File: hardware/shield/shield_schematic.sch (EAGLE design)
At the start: 4 parts, among them IC1 7805TV

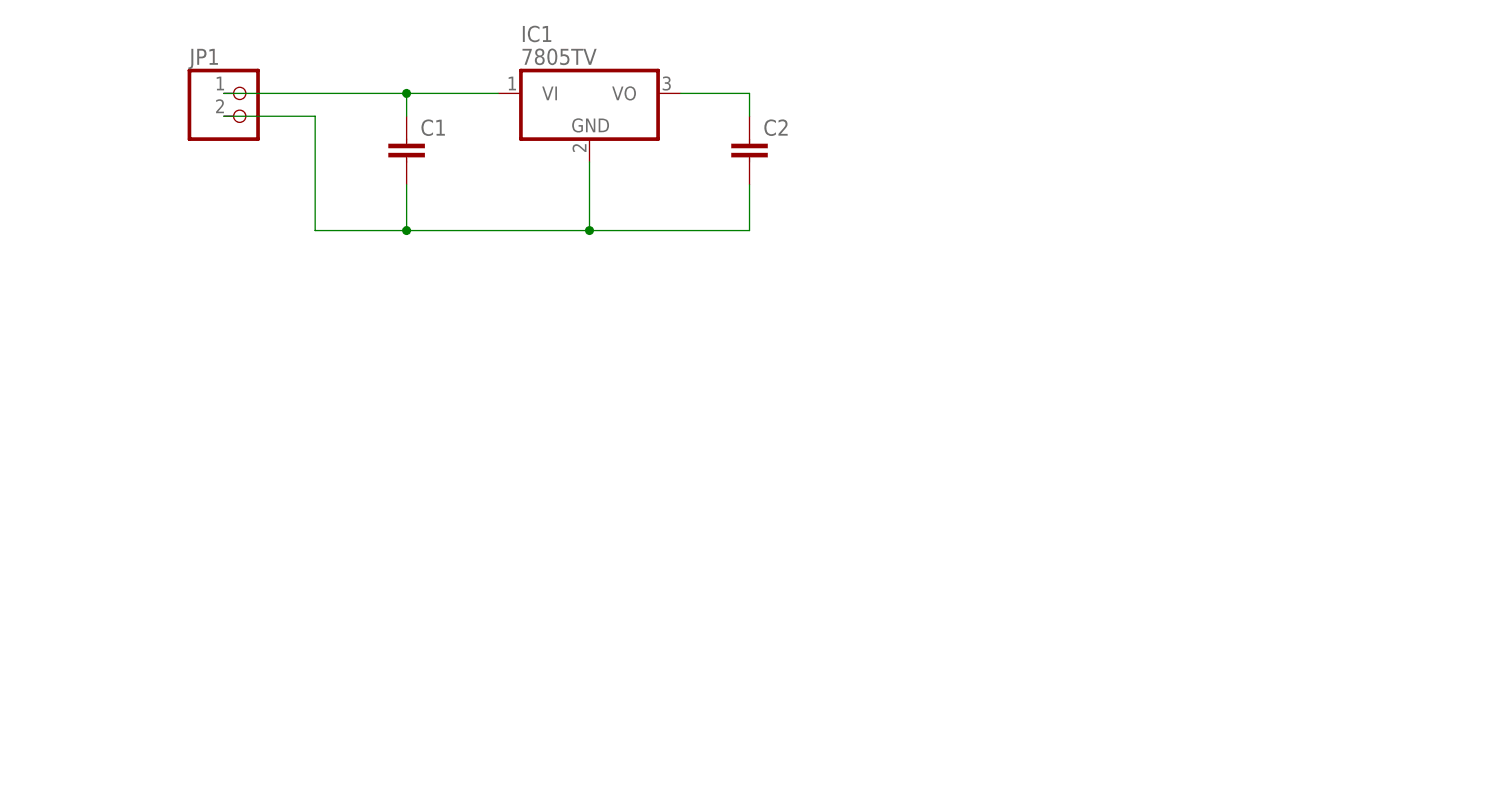
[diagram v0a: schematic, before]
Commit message: Updating the schematics to include A5 frames and complete some component values. Also adding the arduino shield symbol to the shield schematic.
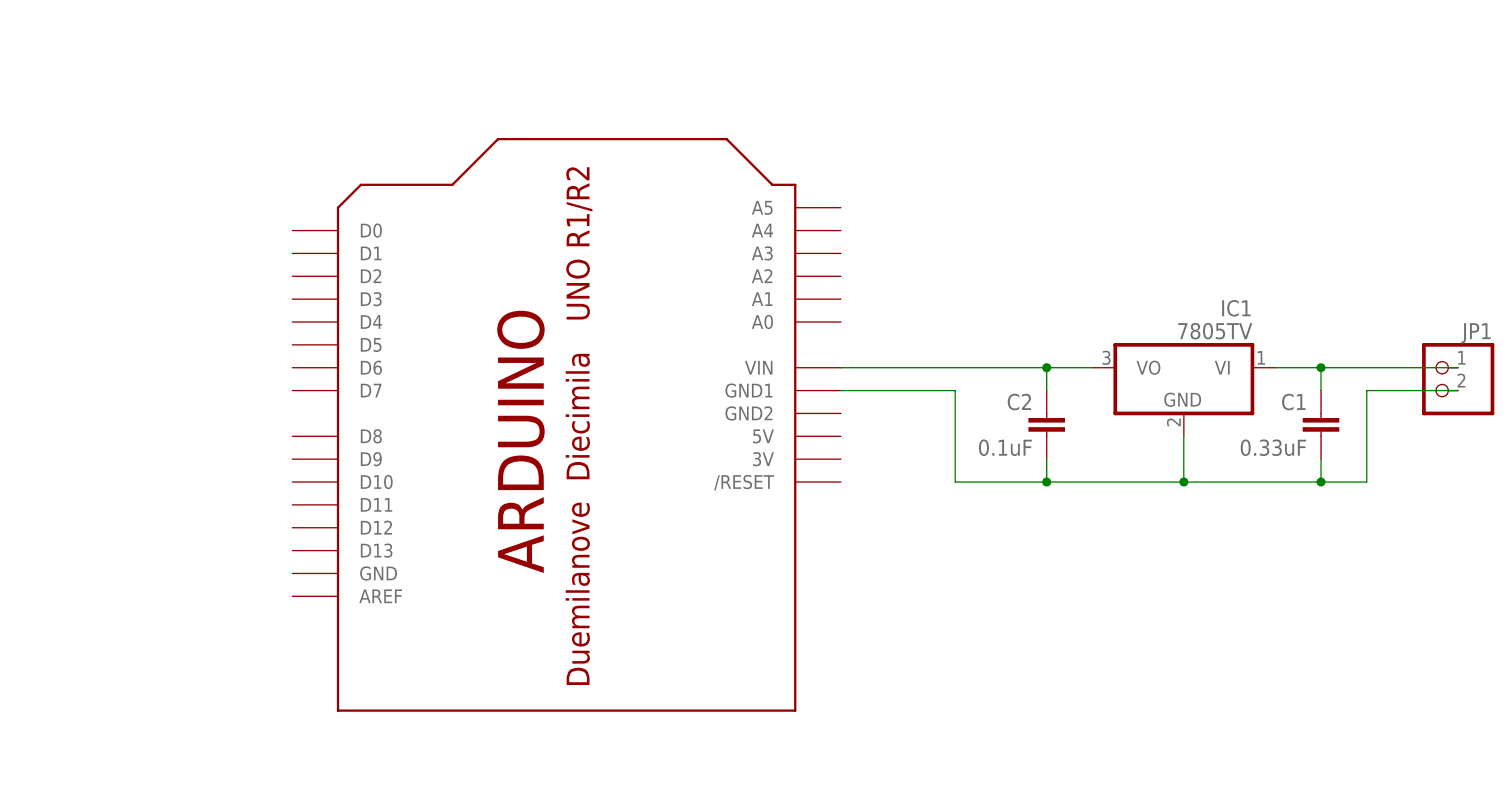
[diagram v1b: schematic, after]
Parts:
- added U$1: ARDUINO-BPLACE, adafruit:ARDUINO-BPLACE
- C1: value (none) -> 0.33uF
- C2: value (none) -> 0.1uF
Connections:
- net N$2: now also U$1.GND1
- net N$3: now also U$1.VIN
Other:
- moved on the sheet: C1, C2, IC1, JP1

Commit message: Update shield schematic: Only uses a single 3.3V regulator. Added the I2C connector and pull ups. Added a note to the SDA UART RX (uC TX) pin used for debugging.
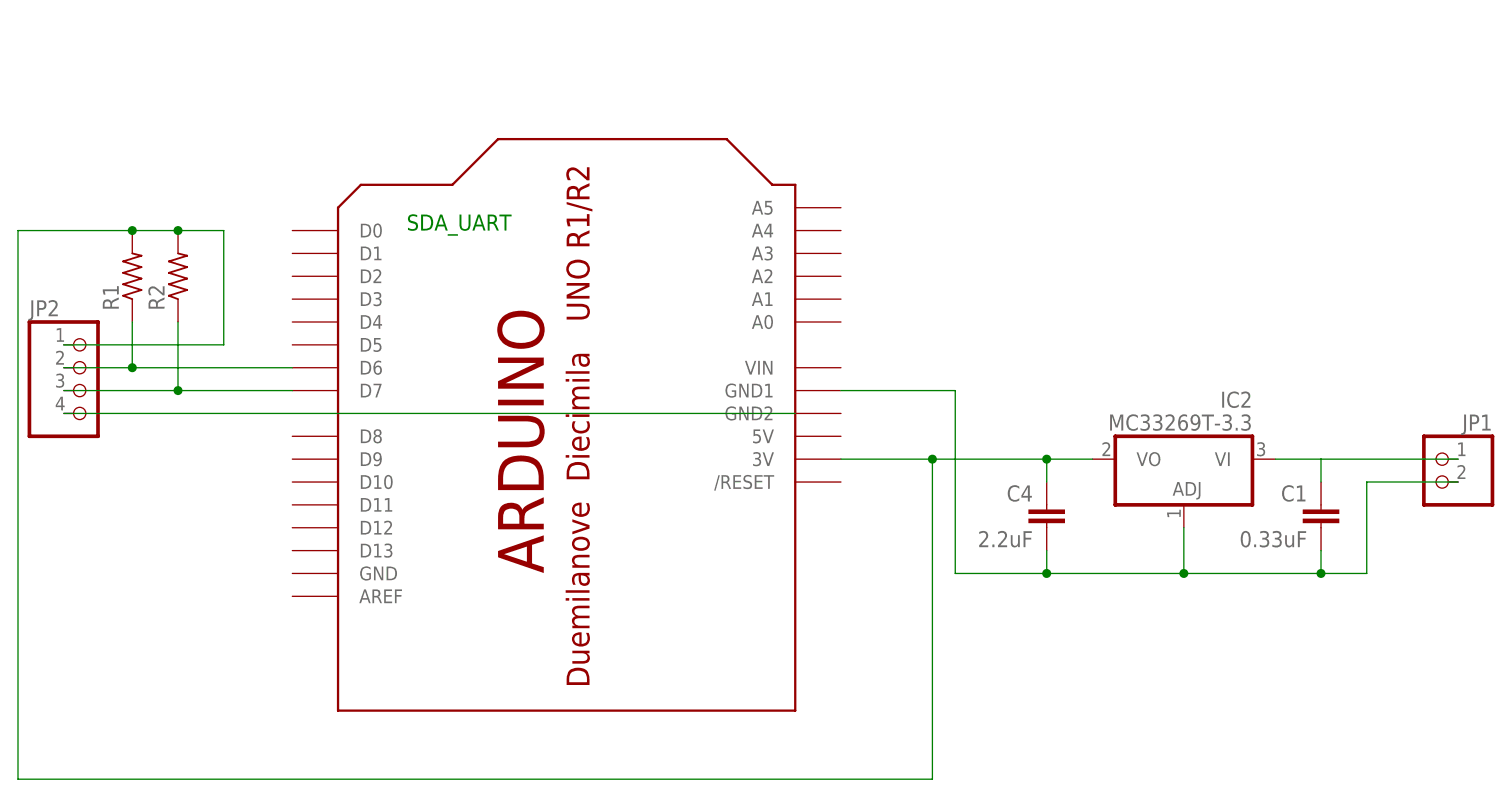
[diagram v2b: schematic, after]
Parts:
- removed C2: 0.1uF, capacitor-wima:C5/2.5
- removed IC1: 7805TV, linear:7805TV
- added C4: 2.2uF, capacitor-wima:C5/2.5
- added IC2: MC33269T-3.3, linear:MC33269T-3.3
- added JP2: (no value), pinhead:PINHD-1X4
- added R1, R2: (no value), resistor:R-US_0204/7
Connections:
- removed net N$3: C2.1, IC1.VO, U$1.VIN
- new net N$4: C4.1, IC2.VO, JP2.1, R1.2, R2.2, U$1.3V
- new net N$5: JP2.2, R1.1, U$1.D6
- new net N$6: JP2.3, R2.1, U$1.D7
- new net N$7: JP2.4
- net N$1: now also IC2.VI; no longer IC1.VI
- net N$2: now also C4.2, IC2.ADJ; no longer C2.2, IC1.GND
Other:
- note added: "SDA_UART"
- moved on the sheet: C1, JP1
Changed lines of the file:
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@@
 </classes>
 <parts>
-<part name="IC1" library="linear" deviceset="78*" device="TV" technology="05"/>
 <part name="C1" library="capacitor-wima" deviceset="C" device="5/2.5" value="0.33uF"/>
-<part name="C2" library="capacitor-wima" deviceset="C" device="5/2.5" value="0.1uF"/>
 <part name="JP1" library="pinhead" deviceset="PINHD-1X2" device=""/>
 <part name="U$1" library="adafruit" deviceset="ARDUINO" device="-BPLACE"/>
 <part name="FRAME2" library="frames" deviceset="DINA5_L" device=""/>
+<part name="IC2" library="linear" deviceset="MC33269?*" device="T" technology="-3.3"/>
+<part name="C4" library="capacitor-wima" deviceset="C" device="5/2.5" value="2.2uF"/>
+<part name="JP2" library="pinhead" deviceset="PINHD-1X4" device=""/>
+<part name="R1" library="resistor" deviceset="R-US_" device="0204/7"/>
+<part name="R2" library="resistor" deviceset="R-US_" device="0204/7"/>
 </parts>
 <sheets>
 <sheet>
 <plain>
+<text x="55.88" y="96.52" size="1.778" layer="91">SDA_UART</text>
 </plain>
 <instances>
-<instance part="IC1" gate="A1" x="142.24" y="81.28" rot="MR0"/>
-<instance part="C1" gate="G$1" x="157.48" y="76.2" rot="MR0"/>
-<instance part="C2" gate="G$1" x="127" y="76.2" rot="MR0"/>
-<instance part="JP1" gate="G$1" x="170.18" y="78.74" rot="MR0"/>
+<instance part="C1" gate="G$1" x="157.48" y="66.04" rot="MR0"/>
+<instance part="JP1" gate="G$1" x="170.18" y="68.58" rot="MR0"/>
 <instance part="U$1" gate="G$1" x="71.12" y="66.04" rot="R90"/>
 <instance part="FRAME2" gate="G$1" x="5.08" y="7.62"/>
+<instance part="IC2" gate="G$1" x="142.24" y="68.58" rot="MR0"/>
+<instance part="C4" gate="G$1" x="127" y="66.04" rot="MR0"/>
+<instance part="JP2" gate="A" x="20.32" y="78.74"/>
+<instance part="R1" gate="G$1" x="25.4" y="91.44" rot="R90"/>
+<instance part="R2" gate="G$1" x="30.48" y="91.44" rot="R90"/>
 </instances>
 <busses>
@@
 <segment>
 <pinref part="JP1" gate="G$1" pin="1"/>
-<pinref part="IC1" gate="A1" pin="VI"/>
-<wire x1="172.72" y1="81.28" x2="157.48" y2="81.28" width="0.1524" layer="91"/>
 <pinref part="C1" gate="G$1" pin="1"/>
-<wire x1="157.48" y1="81.28" x2="152.4" y2="81.28" width="0.1524" layer="91"/>
-<wire x1="157.48" y1="78.74" x2="157.48" y2="81.28" width="0.1524" layer="91"/>
-<junction x="157.48" y="81.28"/>
+<wire x1="172.72" y1="71.12" x2="157.48" y2="71.12" width="0.1524" layer="91"/>
+<wire x1="157.48" y1="68.58" x2="157.48" y2="71.12" width="0.1524" layer="91"/>
+<pinref part="IC2" gate="G$1" pin="VI"/>
+<wire x1="157.48" y1="71.12" x2="152.4" y2="71.12" width="0.1524" layer="91"/>
+</segment>
+</net>
+<net name="N$4" class="0">
+<segment>
+<pinref part="U$1" gate="G$1" pin="3V"/>
+<wire x1="114.3" y1="71.12" x2="104.14" y2="71.12" width="0.1524" layer="91"/>
+<wire x1="114.3" y1="71.12" x2="114.3" y2="35.56" width="0.1524" layer="91"/>
+<pinref part="JP2" gate="A" pin="1"/>
+<wire x1="17.78" y1="83.82" x2="35.56" y2="83.82" width="0.1524" layer="91"/>
+<wire x1="35.56" y1="83.82" x2="35.56" y2="96.52" width="0.1524" layer="91"/>
+<wire x1="35.56" y1="96.52" x2="30.48" y2="96.52" width="0.1524" layer="91"/>
+<wire x1="30.48" y1="96.52" x2="25.4" y2="96.52" width="0.1524" layer="91"/>
+<wire x1="25.4" y1="96.52" x2="12.7" y2="96.52" width="0.1524" layer="91"/>
+<wire x1="12.7" y1="96.52" x2="12.7" y2="35.56" width="0.1524" layer="91"/>
+<wire x1="114.3" y1="35.56" x2="12.7" y2="35.56" width="0.1524" layer="91"/>
+<pinref part="R1" gate="G$1" pin="2"/>
+<junction x="25.4" y="96.52"/>
+<pinref part="R2" gate="G$1" pin="2"/>
+<junction x="30.48" y="96.52"/>
+<pinref part="IC2" gate="G$1" pin="VO"/>
+<wire x1="132.08" y1="71.12" x2="127" y2="71.12" width="0.1524" layer="91"/>
+<pinref part="C4" gate="G$1" pin="1"/>
+<wire x1="127" y1="71.12" x2="114.3" y2="71.12" width="0.1524" layer="91"/>
+<wire x1="127" y1="71.12" x2="127" y2="68.58" width="0.1524" layer="91"/>
+<junction x="127" y="71.12"/>
+<junction x="114.3" y="71.12"/>
+</segment>
+</net>
+<net name="N$5" class="0">
+<segment>
+<pinref part="U$1" gate="G$1" pin="D6"/>
+<pinref part="JP2" gate="A" pin="2"/>
+<wire x1="43.18" y1="81.28" x2="25.4" y2="81.28" width="0.1524" layer="91"/>
+<pinref part="R1" gate="G$1" pin="1"/>
+<wire x1="25.4" y1="81.28" x2="17.78" y2="81.28" width="0.1524" layer="91"/>
+<wire x1="25.4" y1="86.36" x2="25.4" y2="81.28" width="0.1524" layer="91"/>
+<junction x="25.4" y="81.28"/>
+</segment>
+</net>
+<net name="N$6" class="0">
+<segment>
+<pinref part="U$1" gate="G$1" pin="D7"/>
+<pinref part="JP2" gate="A" pin="3"/>
+<wire x1="43.18" y1="78.74" x2="30.48" y2="78.74" width="0.1524" layer="91"/>
+<pinref part="R2" gate="G$1" pin="1"/>
+<wire x1="30.48" y1="78.74" x2="17.78" y2="78.74" width="0.1524" layer="91"/>
+<wire x1="30.48" y1="86.36" x2="30.48" y2="78.74" width="0.1524" layer="91"/>
+<junction x="30.48" y="78.74"/>
+</segment>
+</net>
+<net name="N$7" class="0">
+<segment>
+<pinref part="JP2" gate="A" pin="4"/>
+<wire x1="99.06" y1="76.2" x2="17.78" y2="76.2" width="0.1524" layer="91"/>
 </segment>
 </net>
 <net name="N$2" class="0">
 <segment>
-<pinref part="JP1" gate="G$1" pin="2"/>
-<wire x1="172.72" y1="78.74" x2="162.56" y2="78.74" width="0.1524" layer="91"/>
-<wire x1="162.56" y1="78.74" x2="162.56" y2="68.58" width="0.1524" layer="91"/>
-<wire x1="162.56" y1="68.58" x2="157.48" y2="68.58" width="0.1524" layer="91"/>
-<pinref part="C2" gate="G$1" pin="2"/>
-<wire x1="157.48" y1="68.58" x2="142.24" y2="68.58" width="0.1524" layer="91"/>
-<wire x1="142.24" y1="68.58" x2="127" y2="68.58" width="0.1524" layer="91"/>
-<wire x1="127" y1="68.58" x2="127" y2="71.12" width="0.1524" layer="91"/>
-<pinref part="IC1" gate="A1" pin="GND"/>
-<wire x1="142.24" y1="73.66" x2="142.24" y2="68.58" width="0.1524" layer="91"/>
-<pinref part="C1" gate="G$1" pin="2"/>
-<wire x1="157.48" y1="71.12" x2="157.48" y2="68.58" width="0.1524" layer="91"/>
-<junction x="157.48" y="68.58"/>
-<junction x="142.24" y="68.58"/>
-<wire x1="127" y1="68.58" x2="116.84" y2="68.58" width="0.1524" layer="91"/>
-<wire x1="116.84" y1="68.58" x2="116.84" y2="78.74" width="0.1524" layer="91"/>
 <pinref part="U$1" gate="G$1" pin="GND1"/>
 <wire x1="116.84" y1="78.74" x2="104.14" y2="78.74" width="0.1524" layer="91"/>
-<junction x="127" y="68.58"/>
+<wire x1="116.84" y1="78.74" x2="116.84" y2="58.42" width="0.1524" layer="91"/>
+<pinref part="JP1" gate="G$1" pin="2"/>
+<wire x1="172.72" y1="68.58" x2="162.56" y2="68.58" width="0.1524" layer="91"/>
+<wire x1="162.56" y1="68.58" x2="162.56" y2="58.42" width="0.1524" layer="91"/>
+<wire x1="162.56" y1="58.42" x2="157.48" y2="58.42" width="0.1524" layer="91"/>
+<wire x1="157.48" y1="58.42" x2="142.24" y2="58.42" width="0.1524" layer="91"/>
+<wire x1="142.24" y1="58.42" x2="127" y2="58.42" width="0.1524" layer="91"/>
+<pinref part="C1" gate="G$1" pin="2"/>
+<wire x1="127" y1="58.42" x2="116.84" y2="58.42" width="0.1524" layer="91"/>
+<wire x1="157.48" y1="60.96" x2="157.48" y2="58.42" width="0.1524" layer="91"/>
+<junction x="157.48" y="58.42"/>
+<junction x="142.24" y="58.42"/>
+<pinref part="IC2" gate="G$1" pin="ADJ"/>
+<wire x1="142.24" y1="63.5" x2="142.24" y2="58.42" width="0.1524" layer="91"/>
+<pinref part="C4" gate="G$1" pin="2"/>
+<wire x1="127" y1="60.96" x2="127" y2="58.42" width="0.1524" layer="91"/>
+<junction x="127" y="58.42"/>
 </segment>
 </net>
-<net name="N$3" class="0">
-<segment>
-<pinref part="IC1" gate="A1" pin="VO"/>
-<pinref part="C2" gate="G$1" pin="1"/>
-<wire x1="132.08" y1="81.28" x2="127" y2="81.28" width="0.1524" layer="91"/>
-<wire x1="127" y1="81.28" x2="127" y2="78.74" width="0.1524" layer="91"/>
-<pinref part="U$1" gate="G$1" pin="VIN"/>
-<wire x1="127" y1="81.28" x2="104.14" y2="81.28" width="0.1524" layer="91"/>
-<junction x="127" y="81.28"/>
-</segment>
-</net>
